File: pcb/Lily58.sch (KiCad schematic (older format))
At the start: 119 parts, among them J1 LED, J2 4PIN, P1 i2c_pin, P2 i2c_pin, P3 ICSP, P4 OLED, SW1 SW_PUSH, SW10 SW_PUSH, SW11 SW_PUSH, SW12 SW_PUSH, SW13 SW_PUSH, SW14 SW_PUSH, SW15 SW_PUSH, SW16 SW_PUSH, SW17 SW_PUSH, SW18 SW_PUSH, SW19 SW_PUSH, SW2 SW_PUSH, SW20 SW_PUSH, SW21 SW_PUSH, SW22 SW_PUSH, SW23 SW_PUSH, SW24 SW_PUSH, SW25 SW_PUSH, SW26 SW_PUSH, SW27 SW_PUSH, SW28 SW_PUSH, SW29 SW_PUSH, SW3 SW_PUSH, SW4 SW_PUSH, SW5 SW_PUSH, SW6 SW_PUSH, SW7 SW_PUSH, SW8 SW_PUSH, SW9 SW_PUSH, U1 ProMicro

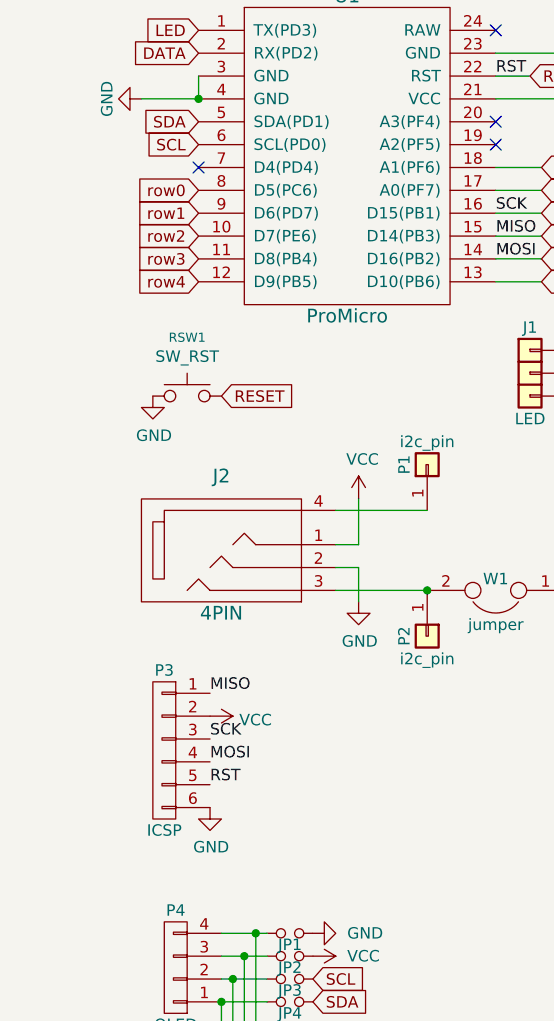
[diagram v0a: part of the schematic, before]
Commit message: add LED for BLE Micro Pro indicator
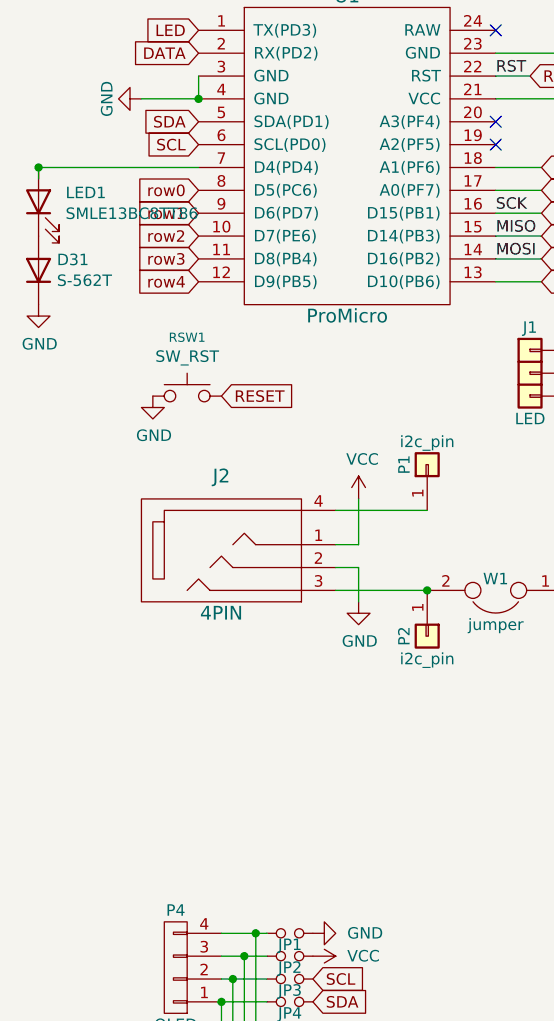
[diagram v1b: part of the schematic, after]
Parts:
- removed P3: ICSP, Lily58-footprint:ICSP, symbol Lily58-rescue:CONN_01X06-Lily58-cache
- added D31: S-562T, Diode_SMD:D_1206_3216Metric_Pad1.42x1.75mm_HandSolder, symbol Device:D
- added LED1: SMLE13BC8TT86, Diode_SMD:D_0603_1608Metric_Pad1.05x0.95mm_HandSolder, symbol Device:LED
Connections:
- net GND: now also D31.1 (K)
- net at U1.7 (D4(PD4)): now also LED1.2 (A)
- new net: D31.2 (A), LED1.1 (K)
- no-connect marks 5 -> 4
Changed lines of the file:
@@
 EESchema Schematic File Version 4
-LIBS:Lily58-cache
-EELAYER 29 0
+EELAYER 30 0
 EELAYER END
 $Descr A3 16535 11693
@@
 Text GLabel 4050 2700 2    50   Input ~ 0
 col0
-NoConn ~ 2550 2700
 $Comp
 L Lily58-rescue:VCC-Lily58-cache #PWR04
@@
 DATA
 Connection ~ 3550 4550
-$Comp
-L Lily58-rescue:CONN_01X06-Lily58-cache P3
-U 1 1 5BB0EA73
-P 2400 5250
-F 0 "P3" H 2400 5600 50  0000 C CNN
-F 1 "ICSP" H 2400 4900 50  0000 C CNN
-F 2 "Lily58-footprint:ICSP" H 2400 5250 50  0001 C CNN
-F 3 "" H 2400 5250 50  0000 C CNN
-	1    2400 5250
-	-1   0    0    -1
-$EndComp
-Text Label 2600 5000 0    50   ~ 0
-MISO
-Text Label 2600 5200 0    50   ~ 0
-SCK
-Text Label 2600 5300 0    50   ~ 0
-MOSI
-Text Label 2600 5400 0    50   ~ 0
-RST
-$Comp
-L power:VCC #PWR0103
-U 1 1 5BB0F35D
-P 2600 5100
-F 0 "#PWR0103" H 2600 4950 50  0001 C CNN
-F 1 "VCC" V 2617 5228 50  0000 L CNN
-F 2 "" H 2600 5100 50  0001 C CNN
-F 3 "" H 2600 5100 50  0001 C CNN
-	1    2600 5100
-	0    1    1    0
-$EndComp
-$Comp
-L power:GND #PWR0104
-U 1 1 5BB0F4C7
-P 2600 5500
-F 0 "#PWR0104" H 2600 5250 50  0001 C CNN
-F 1 "GND" H 2605 5327 50  0000 C CNN
-F 2 "" H 2600 5500 50  0001 C CNN
-F 3 "" H 2600 5500 50  0001 C CNN
-	1    2600 5500
-	1    0    0    -1
-$EndComp
 Text Label 3850 3000 0    50   ~ 0
 MISO
@@
 Wire Wire Line
 	1925 7550 5500 7550
+$Comp
+L power:GND #PWR0103
+U 1 1 61A382E2
+P 1850 3300
+F 0 "#PWR0103" H 1850 3050 50  0001 C CNN
+F 1 "GND" H 1855 3127 50  0000 C CNN
+F 2 "" H 1850 3300 50  0001 C CNN
+F 3 "" H 1850 3300 50  0001 C CNN
+	1    1850 3300
+	1    0    0    -1
+$EndComp
+$Comp
+L Device:D D31
+U 1 1 61A657C6
+P 1850 3150
+F 0 "D31" V 1896 3070 50  0000 R CNN
+F 1 "S-562T" V 1805 3070 50  0000 R CNN
+F 2 "Diode_SMD:D_1206_3216Metric_Pad1.42x1.75mm_HandSolder" H 1850 3150 50  0001 C CNN
+F 3 "~" H 1850 3150 50  0001 C CNN
+	1    1850 3150
+	0    -1   -1   0
+$EndComp
+Wire Wire Line
+	1850 2700 1850 2750
+Wire Wire Line
+	1850 2700 2550 2700
+Connection ~ 1850 2700
+$Comp
+L Device:LED LED1
+U 1 1 61A2AD08
+P 1850 2850
+F 0 "LED1" V 1889 2732 50  0000 R CNN
+F 1 "SMLE13BC8TT86" V 1798 2732 50  0000 R CNN
+F 2 "Diode_SMD:D_0603_1608Metric_Pad1.05x0.95mm_HandSolder" H 1850 2850 50  0001 C CNN
+F 3 "~" H 1850 2850 50  0001 C CNN
+	1    1850 2850
+	0    -1   -1   0
+$EndComp
 $EndSCHEMATC

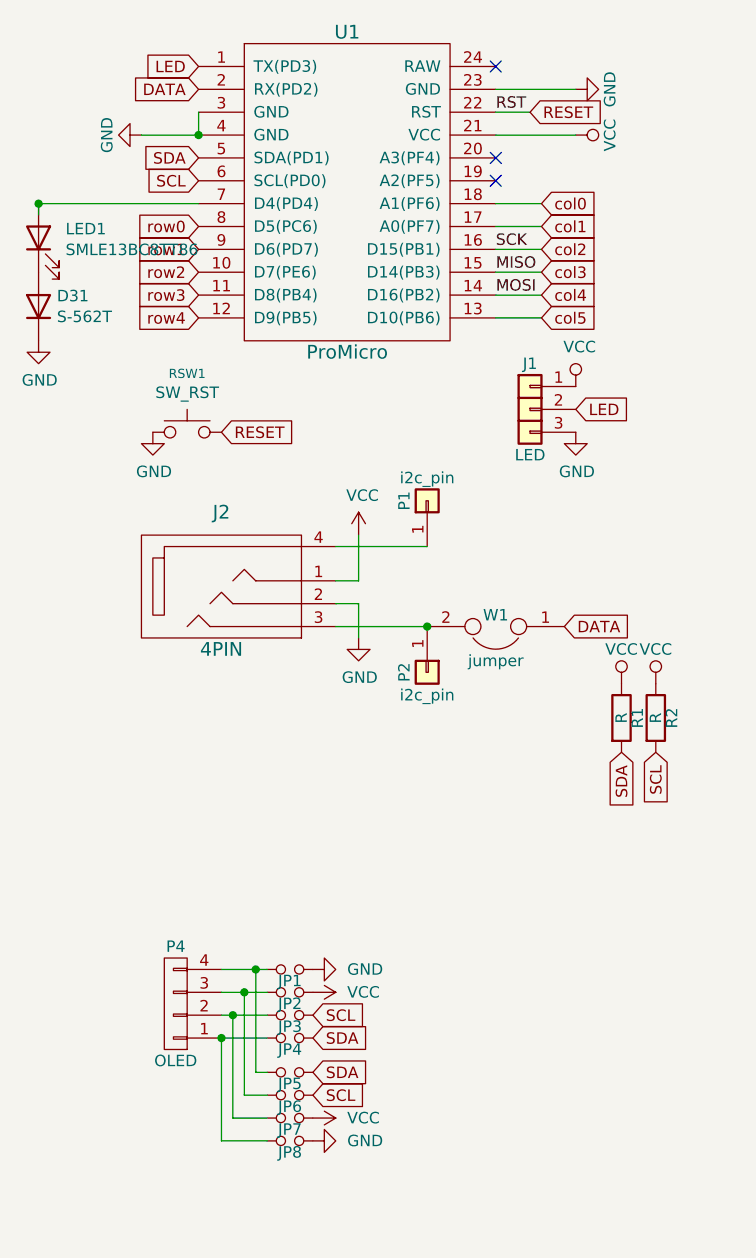
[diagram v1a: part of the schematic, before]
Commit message: change pinsocket 4pin -> 6pin
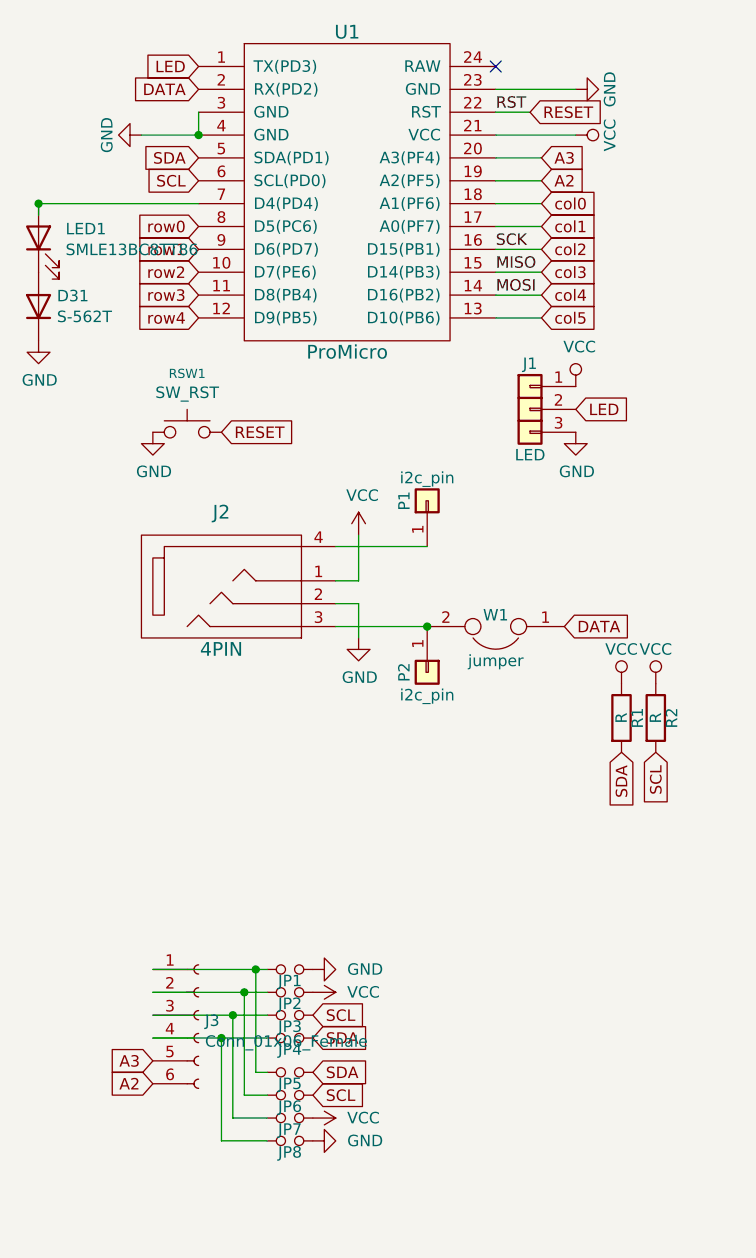
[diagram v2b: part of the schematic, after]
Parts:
- removed P4: OLED, Lily58-footprint:MY_SIL-4, symbol Lily58-rescue:CONN_01X04-Lily58-cache
- added J3: Conn_01x06_Female, Lily58-footprint:OLED_4Pin, symbol Connector:Conn_01x06_Female
- D31: footprint Diode_SMD:D_1206_3216Metric_Pad1.42x1.75mm_HandSolder -> Lily58-footprint:D_1206_3216Metric_Pad1.42x1.75mm_HandSolder
- LED1: footprint Diode_SMD:D_0603_1608Metric_Pad1.05x0.95mm_HandSolder -> Lily58-footprint:LED_0603_1608Metric_Pad1.05x0.95mm_HandSolder
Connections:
- net A2: now reaches U1.19 (A2(PF5))
- net A2: now also J3.6 (Pin_6)
- net A3: now reaches U1.20 (A3(PF4))
- net A3: now also J3.5 (Pin_5)
- net at JP4.1, JP8.1: now also J3.4 (Pin_4)
- net at JP3.1, JP7.1: now also J3.3 (Pin_3)
- net at JP2.1, JP6.1: now also J3.2 (Pin_2)
- net at JP1.1, JP5.1: now also J3.1 (Pin_1)
- no-connect marks 4 -> 2
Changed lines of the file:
@@
 Text GLabel 2550 2100 0    50   Input ~ 0
 LED
-NoConn ~ 3850 2600
 Text GLabel 2550 2600 0    50   Input ~ 0
 SCL
 Text GLabel 2550 2500 0    50   Input ~ 0
 SDA
-NoConn ~ 3850 2500
 Text GLabel 2550 2800 0    50   Input ~ 0
 row0
@@
 	4200 2400 3850 2400
 $Comp
-L Lily58-rescue:CONN_01X04-Lily58-cache P4
-U 1 1 5BE5032C
-P 2450 6200
-F 0 "P4" H 2450 5950 50  0000 C CNN
-F 1 "OLED" H 2450 6450 50  0000 C CNN
-F 2 "Lily58-footprint:MY_SIL-4" H 2450 6200 50  0001 C CNN
-F 3 "" H 2450 6200 50  0000 C CNN
-	1    2450 6200
-	-1   0    0    1
-$EndComp
-$Comp
 L power:GND #PWR03
 U 1 1 5BE50789
@@
 	0    1    1    0
 $EndComp
-Wire Wire Line
-	2650 6050 2800 6050
-Wire Wire Line
-	2650 6150 2750 6150
-Wire Wire Line
-	2650 6250 2700 6250
 Text GLabel 3050 6250 2    50   Input ~ 0
 SCL
@@
 Wire Wire Line
 	2650 6350 2850 6350
-Connection ~ 2650 6350
 Wire Wire Line
 	2850 6500 2800 6500
@@
 F 0 "D31" V 1896 3070 50  0000 R CNN
 F 1 "S-562T" V 1805 3070 50  0000 R CNN
-F 2 "Diode_SMD:D_1206_3216Metric_Pad1.42x1.75mm_HandSolder" H 1850 3150 50  0001 C CNN
+F 2 "Lily58-footprint:D_1206_3216Metric_Pad1.42x1.75mm_HandSolder" H 1850 3150 50  0001 C CNN
 F 3 "~" H 1850 3150 50  0001 C CNN
 	1    1850 3150
@@
 F 0 "LED1" V 1889 2732 50  0000 R CNN
 F 1 "SMLE13BC8TT86" V 1798 2732 50  0000 R CNN
-F 2 "Diode_SMD:D_0603_1608Metric_Pad1.05x0.95mm_HandSolder" H 1850 2850 50  0001 C CNN
+F 2 "Lily58-footprint:LED_0603_1608Metric_Pad1.05x0.95mm_HandSolder" H 1850 2850 50  0001 C CNN
 F 3 "~" H 1850 2850 50  0001 C CNN
 	1    1850 2850
 	0    -1   -1   0
 $EndComp
+$Comp
+L Connector:Conn_01x06_Female J3
+U 1 1 6192B632
+P 2550 6250
+F 0 "J3" H 2578 6226 50  0000 L CNN
+F 1 "Conn_01x06_Female" H 2578 6135 50  0000 L CNN
+F 2 "Lily58-footprint:OLED_4Pin" H 2550 6250 50  0001 C CNN
+F 3 "~" H 2550 6250 50  0001 C CNN
+	1    2550 6250
+	1    0    0    -1
+$EndComp
+Wire Wire Line
+	2350 6050 2800 6050
+Wire Wire Line
+	2350 6150 2750 6150
+Wire Wire Line
+	2350 6250 2700 6250
+Wire Wire Line
+	2650 6350 2350 6350
+Connection ~ 2650 6350
+Wire Wire Line
+	3850 2500 4050 2500
+Wire Wire Line
+	3850 2600 4050 2600
+Text GLabel 4050 2500 2    50   Input ~ 0
+A3
+Text GLabel 4050 2600 2    50   Input ~ 0
+A2
+Text GLabel 2350 6450 0    50   Input ~ 0
+A3
+Text GLabel 2350 6550 0    50   Input ~ 0
+A2
 $EndSCHEMATC

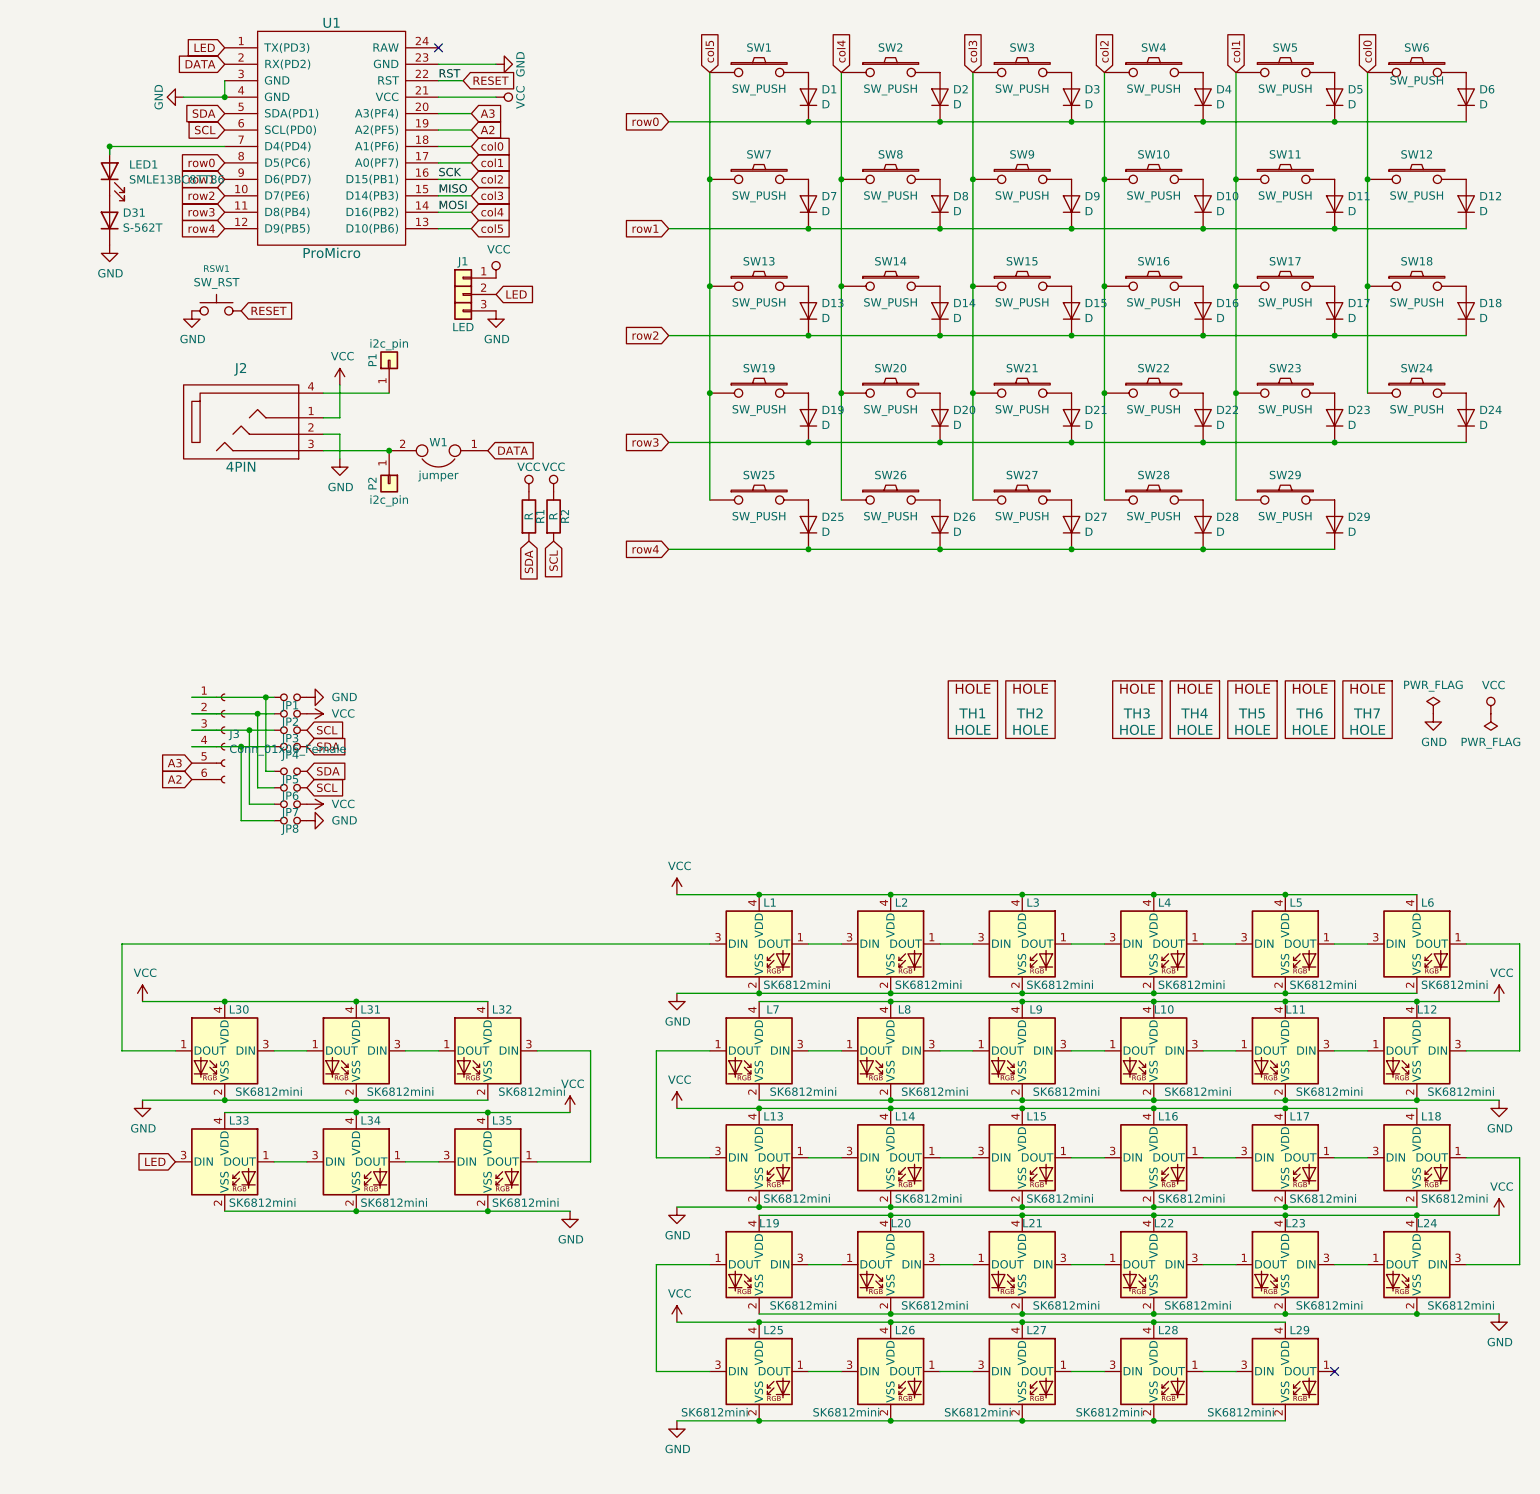
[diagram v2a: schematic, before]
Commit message: change pad and delete underglow
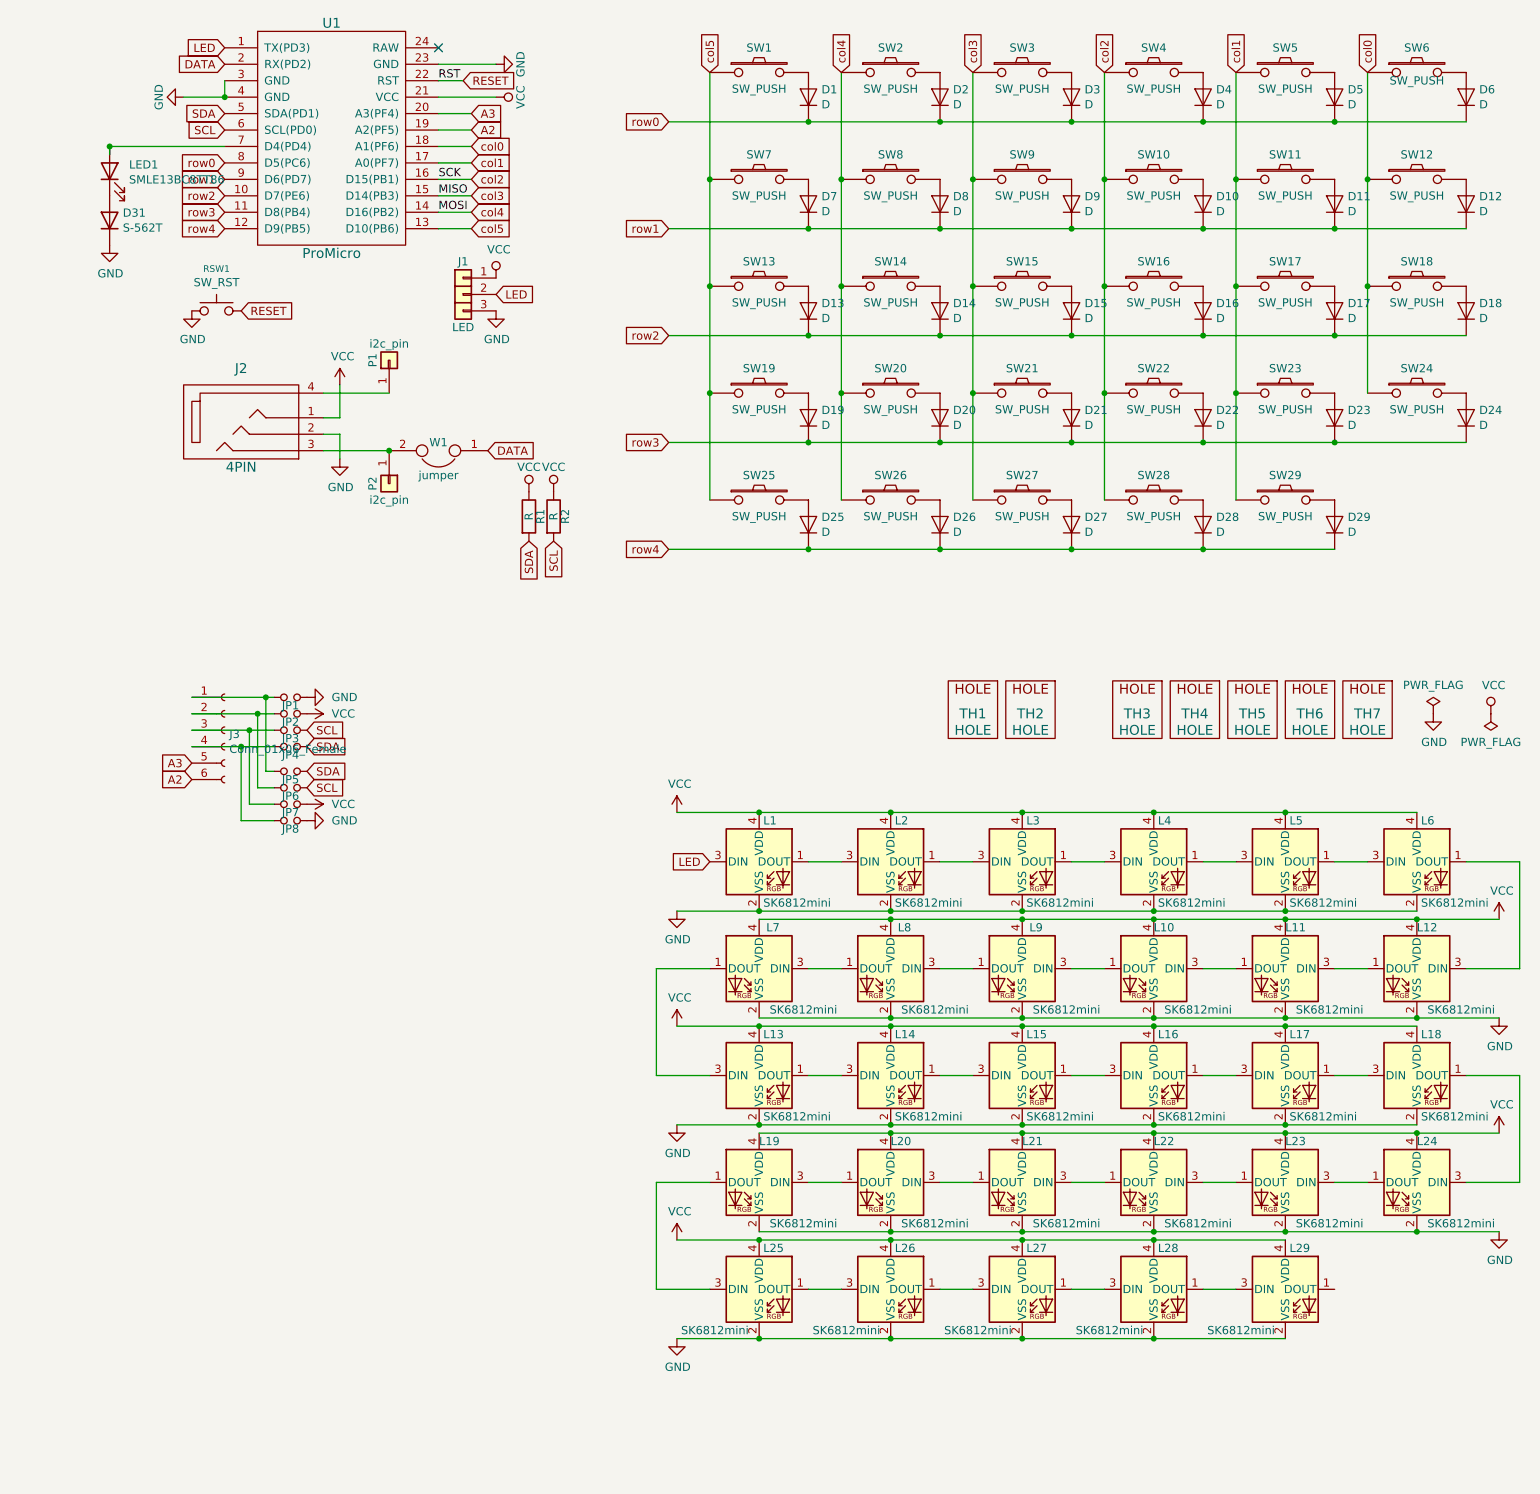
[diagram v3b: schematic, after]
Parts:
- removed L30, L31, L32, L33, L34, L35: SK6812mini, Lily58-footprint:SK6812MINI_underglow_rev, symbol LED:SK6812MINI
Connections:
- net LED: now also L1.3 (DIN)
- no-connect marks 2 -> 1
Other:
- moved on the sheet: L1, L10, L11, L12, L13, L14, L15, L16, L17, L18, L19, L2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
